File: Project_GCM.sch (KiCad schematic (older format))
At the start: 20 parts, among them J1 Alimentation, J12 DEBUG_BUSES, J7 3-641124-6, U1 LM810, U11 74AHC1G04, U2 LTC6994xS6-1, U25 74AHC1G32, U3 74AHC1G32, U5 74AHC1G04

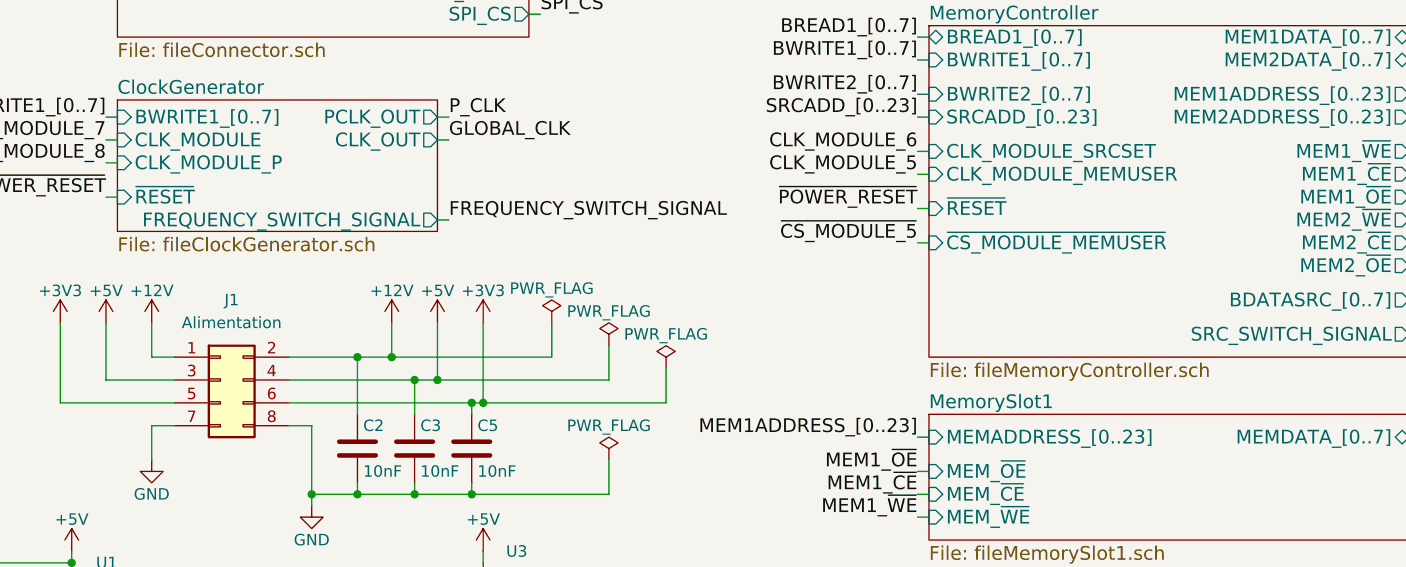
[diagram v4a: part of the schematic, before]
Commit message: Update materials list, begin to work on pcb
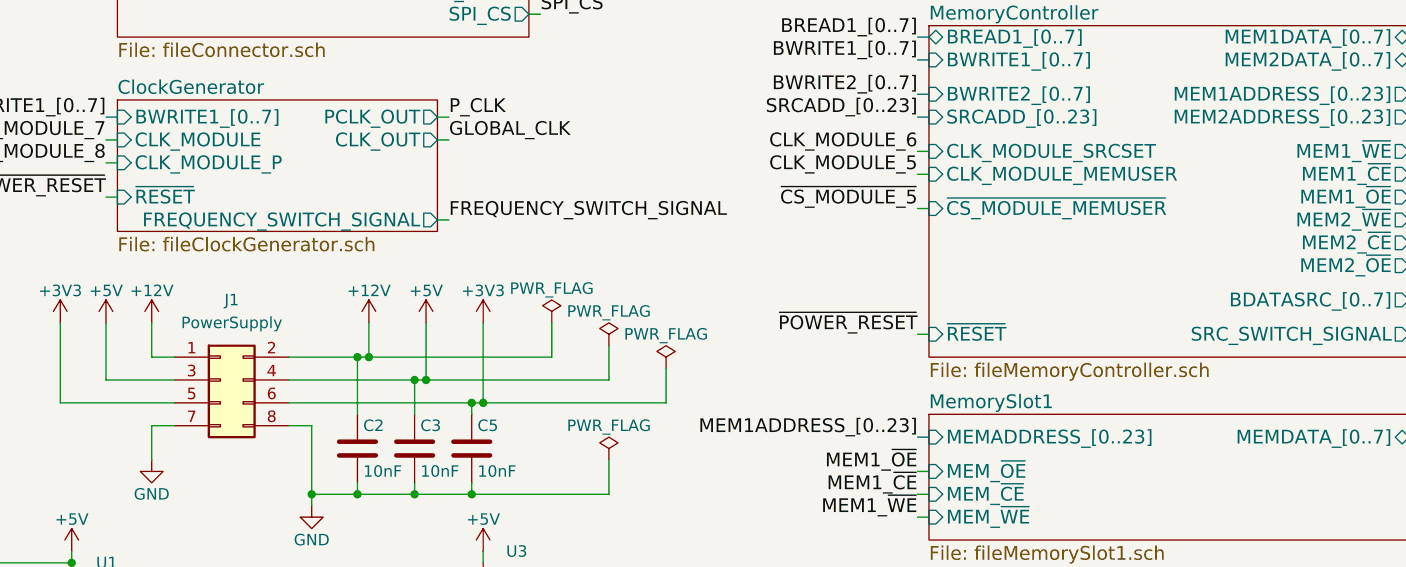
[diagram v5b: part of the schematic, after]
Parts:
- J1: value Alimentation -> PowerSupply
- U11, U25, U3, U5: footprint (none) -> Package_TO_SOT_SMD:SOT-23-5
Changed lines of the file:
@@
 L power:+12V #PWR01
 U 1 1 5B3CC2AA
-P 2500 3550
-F 0 "#PWR01" H 2500 3400 50  0001 C CNN
-F 1 "+12V" H 2500 3690 50  0000 C CNN
-F 2 "" H 2500 3550 50  0001 C CNN
-F 3 "" H 2500 3550 50  0001 C CNN
-	1    2500 3550
+P 2400 3550
+F 0 "#PWR01" H 2400 3400 50  0001 C CNN
+F 1 "+12V" H 2400 3690 50  0000 C CNN
+F 2 "" H 2400 3550 50  0001 C CNN
+F 3 "" H 2400 3550 50  0001 C CNN
+	1    2400 3550
 	1    0    0    -1
 $EndComp
@@
 L power:+5V #PWR02
 U 1 1 5B3CE793
-P 2700 3550
-F 0 "#PWR02" H 2700 3400 50  0001 C CNN
-F 1 "+5V" H 2700 3690 50  0000 C CNN
-F 2 "" H 2700 3550 50  0001 C CNN
-F 3 "" H 2700 3550 50  0001 C CNN
-	1    2700 3550
+P 2650 3550
+F 0 "#PWR02" H 2650 3400 50  0001 C CNN
+F 1 "+5V" H 2650 3690 50  0000 C CNN
+F 2 "" H 2650 3550 50  0001 C CNN
+F 3 "" H 2650 3550 50  0001 C CNN
+	1    2650 3550
 	1    0    0    -1
 $EndComp
@@
 $EndComp
 Wire Wire Line
-	2500 3700 2500 3550
-Wire Wire Line
-	2700 3800 2700 3550
+	2400 3700 2400 3550
+Wire Wire Line
+	2650 3800 2650 3550
 Wire Wire Line
 	2900 3900 2900 3550
@@
 F18 "CLK_MODULE_SRCSET" I L 4850 2800 60
 F19 "CLK_MODULE_MEMUSER" I L 4850 2900 60
-F20 "~RESET" I L 4850 3050 60
-F21 "~CS_MODULE_MEMUSER" I L 4850 3200 60
+F20 "~RESET" I L 4850 3600 60
+F21 "~CS_MODULE_MEMUSER" I L 4850 3050 60
 $EndSheet
 Text Label 6500 1200 0    60   ~ 0
@@
 Wire Wire Line
 	3200 3700 3200 3550
-Connection ~ 2500 3700
 Wire Wire Line
 	3450 3800 3450 3650
-Connection ~ 2700 3800
 Wire Wire Line
 	3700 3900 3700 3750
@@
 	2850 3900 2900 3900
 Wire Wire Line
-	2600 3800 2700 3800
-Wire Wire Line
-	2350 3700 2500 3700
+	2600 3800 2650 3800
+Wire Wire Line
+	2350 3700 2400 3700
 Wire Wire Line
 	2150 4300 2150 4350
@@
 Wire Wire Line
 	2350 4300 2600 4300
-Wire Wire Line
-	2500 3700 3200 3700
-Wire Wire Line
-	2700 3800 3450 3800
 Wire Wire Line
 	2900 3900 3700 3900
@@
 P 1750 3800
 F 0 "J1" H 1800 4150 50  0000 C CNN
-F 1 "Alimentation" H 1800 4050 50  0000 C CNN
+F 1 "PowerSupply" H 1800 4050 50  0000 C CNN
 F 2 "Connector_Molex:Molex_Nano-Fit_105310-xx08_2x04_P2.50mm_Vertical" H 1750 3800 50  0001 C CNN
 F 3 "~" H 1750 3800 50  0001 C CNN
@@
 Wire Bus Line
 	6950 2400 7000 2400
-Text Label 4800 3200 2    60   ~ 0
+Text Label 4800 3050 2    60   ~ 0
 ~CS_MODULE_5
 Text Label 4800 2800 2    60   ~ 0
@@
 F 0 "U5" H 3900 6500 50  0000 L CNN
 F 1 "74AHC1G04" H 3900 6400 50  0000 L CNN
-F 2 "" H 3800 6250 50  0001 C CNN
+F 2 "Package_TO_SOT_SMD:SOT-23-5" H 3800 6250 50  0001 C CNN
 F 3 "https://assets.nexperia.com/documents/data-sheet/74AHC_AHCT1G04.pdf" H 3800 6250 50  0001 C CNN
 	1    3800 6250
@@
 F 0 "U11" H 5850 6500 50  0000 L CNN
 F 1 "74AHC1G04" H 5850 6400 50  0000 L CNN
-F 2 "" H 5750 6250 50  0001 C CNN
+F 2 "Package_TO_SOT_SMD:SOT-23-5" H 5750 6250 50  0001 C CNN
 F 3 "https://assets.nexperia.com/documents/data-sheet/74AHC_AHCT1G04.pdf" H 5750 6250 50  0001 C CNN
 	1    5750 6250
@@
 F 0 "U3" H 3000 5050 50  0000 L CNN
 F 1 "74AHC1G32" H 3000 4950 50  0000 L CNN
-F 2 "" H 2900 4800 50  0001 C CNN
+F 2 "Package_TO_SOT_SMD:SOT-23-5" H 2900 4800 50  0001 C CNN
 F 3 "http://www.ti.com/lit/sg/scyt129e/scyt129e.pdf" H 2900 4800 50  0001 C CNN
 	1    2900 4800
@@
 Text Label 6050 6250 0    60   ~ 0
 ~POWER_RESET
-Text Label 4800 3050 2    60   ~ 0
+Text Label 4800 3600 2    60   ~ 0
 ~POWER_RESET
 Text Label 2500 6900 0    60   ~ 0
@@
 F 0 "U25" H 3000 5950 50  0000 L CNN
 F 1 "74AHC1G32" H 3000 5850 50  0000 L CNN
-F 2 "" H 2900 5700 50  0001 C CNN
+F 2 "Package_TO_SOT_SMD:SOT-23-5" H 2900 5700 50  0001 C CNN
 F 3 "http://www.ti.com/lit/sg/scyt129e/scyt129e.pdf" H 2900 5700 50  0001 C CNN
 	1    2900 5700
@@
 	4800 2900 4850 2900
 Wire Wire Line
+	4800 3600 4850 3600
+Wire Wire Line
 	4800 3050 4850 3050
-Wire Wire Line
-	4800 3200 4850 3200
 Text Label 4800 2550 2    60   ~ 0
 BWRITE2_[0..7]
 NoConn ~ 6500 1700
+Connection ~ 2650 3800
+Wire Wire Line
+	2650 3800 3450 3800
+Connection ~ 2400 3700
+Wire Wire Line
+	2400 3700 3200 3700
 Wire Bus Line
 	9000 1750 9000 2500
